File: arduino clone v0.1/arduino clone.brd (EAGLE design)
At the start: 68.6 x 26.2 mm, 47 parts, among them J203 ICSP HEADER, J402 FTDI Breakout Header, U101 ATMEGA328P_TQFP, U301 CH340G, Y101 16MHz, Y301 12MHz

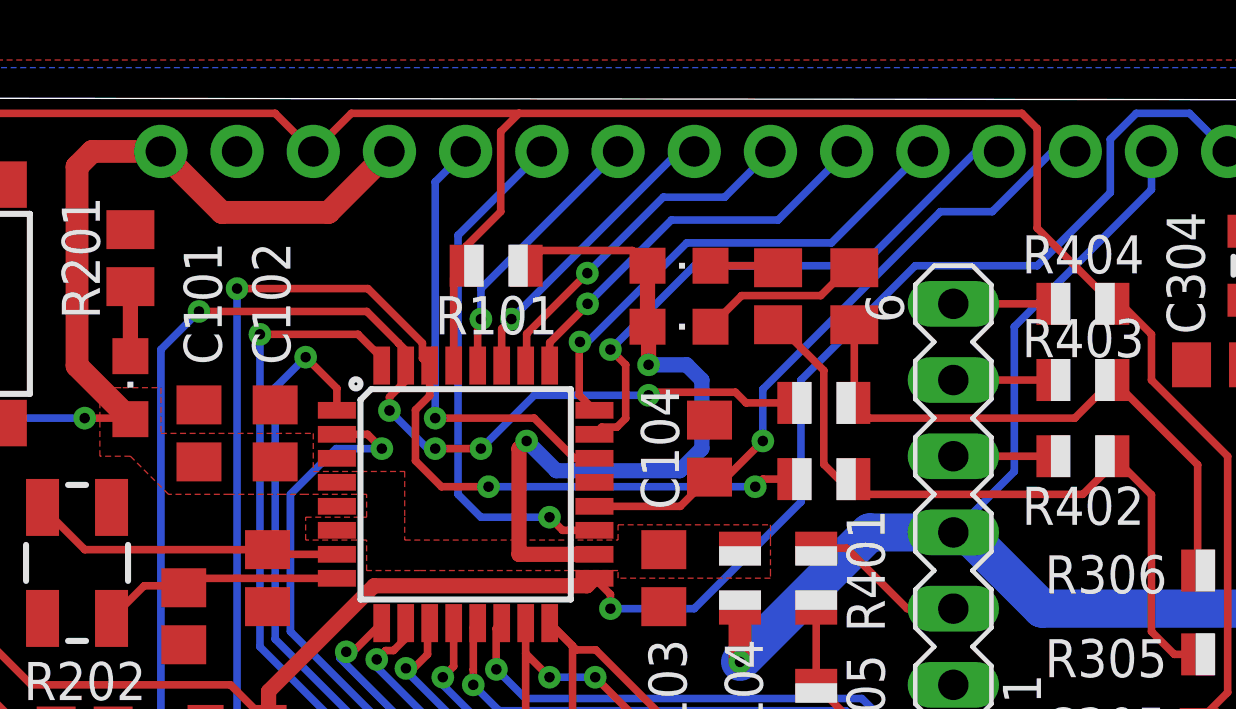
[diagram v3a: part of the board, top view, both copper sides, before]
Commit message: add gnd vias so gnd hits everything
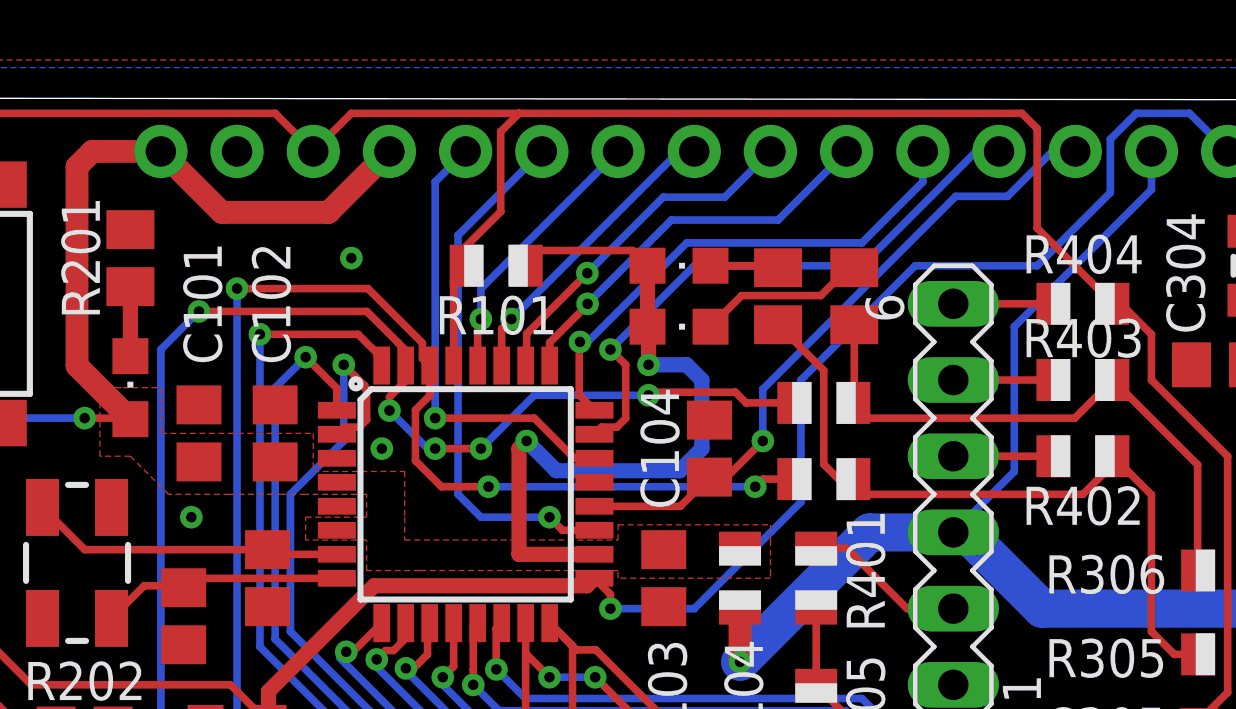
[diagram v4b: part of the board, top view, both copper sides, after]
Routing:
- net MCU_D4: track 23.7 -> 26.7 mm
- net MCU_A1: track 16.6 -> 17.2 mm
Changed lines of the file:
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@@
 <vertex x="82.042" y="66.294"/>
 </polygon>
-<wire x1="72.771" y1="50.193" x2="76.802" y2="53.37" width="0" layer="19" extent="1-1"/>
-<wire x1="70.8" y1="52.324" x2="72.771" y2="50.193" width="0" layer="19" extent="1-1"/>
-<wire x1="76.642" y1="43.942" x2="72.771" y2="50.193" width="0" layer="19" extent="1-1"/>
-<wire x1="68.85" y1="60.452" x2="70.8" y2="52.324" width="0" layer="19" extent="1-1"/>
-<wire x1="61.026" y1="53.848" x2="70.8" y2="52.324" width="0" layer="19" extent="1-1"/>
-<wire x1="58.486" y1="56.388" x2="61.026" y2="53.848" width="0" layer="19" extent="1-1"/>
-<wire x1="66.294" y1="40.402" x2="76.642" y2="43.942" width="0" layer="19" extent="1-1"/>
-<wire x1="50.546" y1="45.72" x2="61.026" y2="53.848" width="0" layer="19" extent="1-1"/>
-<wire x1="45.974" y1="43.704" x2="50.546" y2="45.72" width="0" layer="19" extent="1-1"/>
-<wire x1="40.894" y1="48.326" x2="45.974" y2="43.704" width="0" layer="19" extent="1-1"/>
+<via x="30.48" y="59.944" extent="1-16" drill="0.35"/>
+<via x="25.146" y="51.308" extent="1-16" drill="0.35"/>
+<via x="31.496" y="53.594" extent="1-16" drill="0.35"/>
 <wire x1="38.5826" y1="52.47" x2="40.894" y2="48.326" width="0" layer="19" extent="1-1"/>
-<wire x1="42.418" y1="54.544" x2="38.5826" y2="52.47" width="0" layer="19" extent="1-1"/>
-<wire x1="29.9974" y1="51.67" x2="38.5826" y2="52.47" width="0" layer="19" extent="1-1"/>
-<wire x1="29.9974" y1="53.27" x2="29.9974" y2="51.67" width="0" layer="19" extent="1-1"/>
-<wire x1="27.94" y1="55.052" x2="29.9974" y2="53.27" width="0" layer="19" extent="1-1"/>
-<wire x1="25.4" y1="55.052" x2="27.94" y2="55.052" width="0" layer="19" extent="1-1"/>
-<wire x1="27.686" y1="48.326" x2="29.9974" y2="51.67" width="0" layer="19" extent="1-1"/>
-<wire x1="24.892" y1="47.056" x2="27.686" y2="48.326" width="0" layer="19" extent="1-1"/>
-<wire x1="20.64" y1="44.196" x2="24.892" y2="47.056" width="0" layer="19" extent="1-1"/>
-<wire x1="23.114" y1="60.894" x2="25.4" y2="55.052" width="0" layer="19" extent="1-1"/>
-<wire x1="26.67" y1="63.5" x2="23.114" y2="60.894" width="0" layer="19" extent="1-1"/>
-<wire x1="14.224" y1="49.53" x2="20.64" y2="44.196" width="0" layer="19" extent="1-1"/>
-<wire x1="14.514" y1="54.445" x2="14.224" y2="49.53" width="0" layer="19" extent="1-1"/>
-<wire x1="31.75" y1="40.64" x2="27.686" y2="48.326" width="0" layer="19" extent="1-1"/>
 </signal>
 <signal name="MCU_RESET">
@@
 <via x="44.196" y="53.848" extent="1-16" drill="0.35"/>
 <wire x1="53.848" y1="63.5" x2="54.61" y2="63.5" width="0.254" layer="16"/>
-<wire x1="44.196" y1="55.5747625" x2="50.1146375" y2="61.4934" width="0.254" layer="16"/>
-<wire x1="50.1146375" y1="61.4934" x2="51.8414" y2="61.4934" width="0.254" layer="16"/>
-<wire x1="51.8414" y1="61.4934" x2="53.848" y2="63.5" width="0.254" layer="16"/>
+<wire x1="44.196" y1="55.5747625" x2="50.6226375" y2="62.0014" width="0.254" layer="16"/>
+<wire x1="50.6226375" y1="62.0014" x2="52.3494" y2="62.0014" width="0.254" layer="16"/>
+<wire x1="52.3494" y1="62.0014" x2="53.848" y2="63.5" width="0.254" layer="16"/>
 <wire x1="44.196" y1="53.848" x2="44.196" y2="55.5747625" width="0.254" layer="16"/>
 </signal>
@@
 <wire x1="38.354" y1="57.15" x2="38.1" y2="57.15" width="0.254" layer="16"/>
 <wire x1="38.354" y1="57.15" x2="41.656" y2="60.452" width="0.254" layer="16"/>
-<wire x1="46.482" y1="60.452" x2="41.656" y2="60.452" width="0.254" layer="16"/>
-<wire x1="49.53" y1="63.5" x2="46.482" y2="60.452" width="0.254" layer="16"/>
+<wire x1="47.498" y1="60.452" x2="41.656" y2="60.452" width="0.254" layer="16"/>
+<wire x1="49.53" y1="62.484" x2="47.498" y2="60.452" width="0.254" layer="16"/>
 <wire x1="38.5826" y1="54.87" x2="38.0746" y2="55.378" width="0.254" layer="1"/>
 <wire x1="38.0746" y1="57.1246" x2="38.1" y2="57.15" width="0.254" layer="1"/>
+<wire x1="49.53" y1="63.5" x2="49.53" y2="62.484" width="0.254" layer="16"/>
 </signal>
 <signal name="MCU_A2">
@@
 <contactref element="U101" pad="2"/>
 <contactref element="J201" pad="7"/>
-<wire x1="29.9974" y1="54.07" x2="31.02" y2="54.07" width="0.254" layer="1"/>
-<wire x1="31.02" y1="54.07" x2="31.496" y2="53.594" width="0.254" layer="1"/>
-<via x="31.496" y="53.594" extent="1-16" drill="0.35"/>
 <wire x1="28.448" y1="52.07" x2="28.448" y2="48.514" width="0.254" layer="16"/>
-<wire x1="29.972" y1="53.594" x2="28.448" y2="52.07" width="0.254" layer="16"/>
-<wire x1="31.496" y1="53.594" x2="29.972" y2="53.594" width="0.254" layer="16"/>
+<wire x1="30.226" y1="53.848" x2="28.448" y2="52.07" width="0.254" layer="16"/>
 <wire x1="28.448" y1="48.514" x2="28.448" y2="48.514" width="0.254" layer="16"/>
 <wire x1="28.448" y1="48.514" x2="28.448" y2="47.498" width="0.254" layer="16"/>
@@
 <wire x1="35.56" y1="42.672" x2="36.4236" y2="41.8084" width="0.254" layer="16"/>
 <wire x1="33.274" y1="42.672" x2="35.56" y2="42.672" width="0.254" layer="16"/>
+<wire x1="29.9974" y1="54.07" x2="30.2386" y2="54.3112" width="0.254" layer="1"/>
+<wire x1="30.2386" y1="54.3112" x2="30.74813125" y2="54.3112" width="0.254" layer="1"/>
+<wire x1="30.74813125" y1="54.3112" x2="30.988" y2="54.55106875" width="0.254" layer="1"/>
+<wire x1="30.988" y1="55.55506875" x2="30.9312" y2="55.61186875" width="0.254" layer="1"/>
+<wire x1="30.9312" y1="55.61186875" x2="30.9312" y2="55.6828" width="0.254" layer="1"/>
+<wire x1="30.9312" y1="55.6828" x2="30.226" y2="56.388" width="0.254" layer="1"/>
+<wire x1="30.988" y1="54.55106875" x2="30.988" y2="55.55506875" width="0.254" layer="1"/>
+<via x="30.226" y="56.388" extent="1-16" drill="0.35"/>
+<wire x1="30.226" y1="56.388" x2="30.226" y2="53.848" width="0.254" layer="16"/>
 </signal>
 <signal name="MCU_D5">

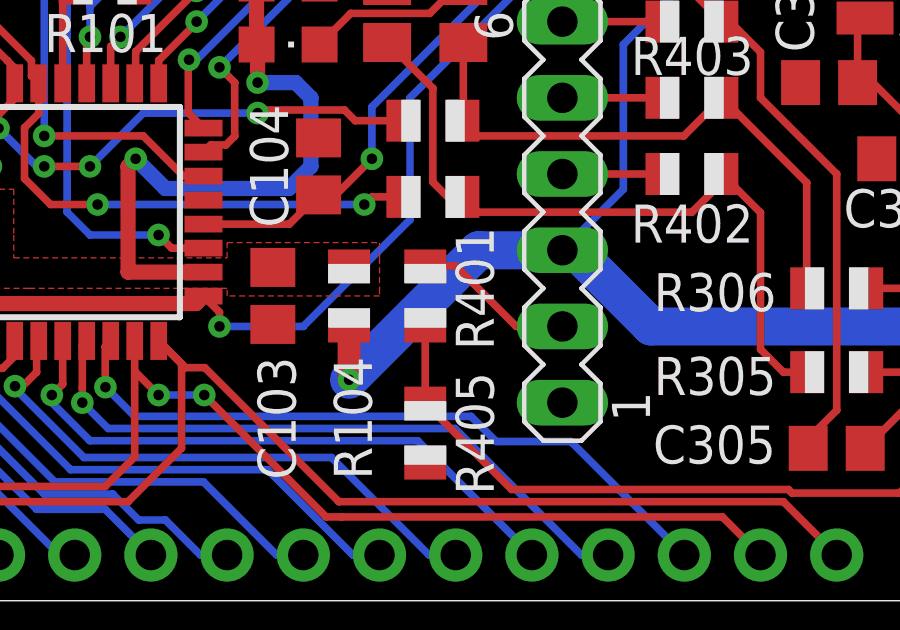
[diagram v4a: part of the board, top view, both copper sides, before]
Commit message: add shape for PP5V0_USB to MCU
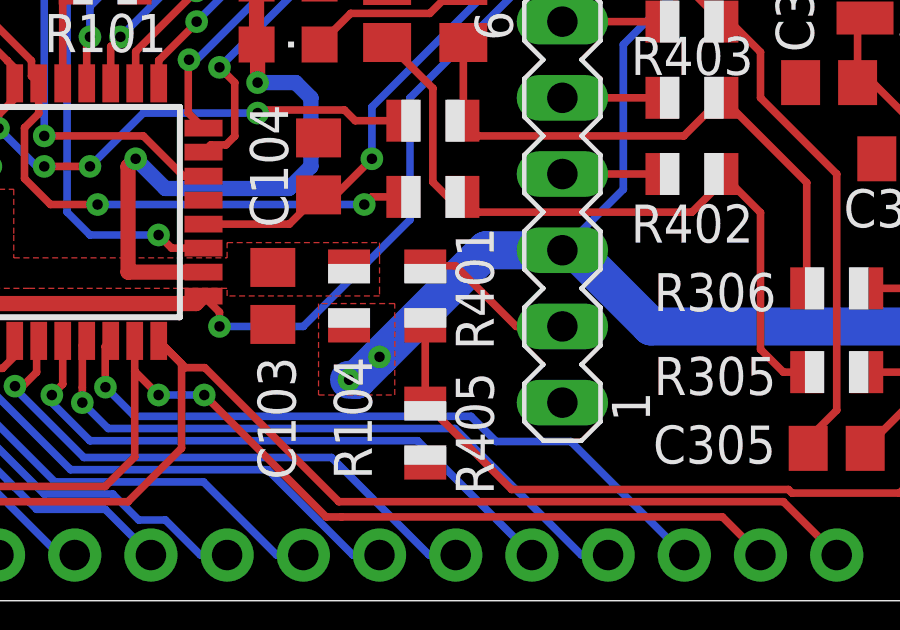
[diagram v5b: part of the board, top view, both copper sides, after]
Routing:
- net PP5V0_USB: track 65.3 -> 63.5 mm, vias 2 -> 3
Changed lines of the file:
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@@
 <via x="25.146" y="51.308" extent="1-16" drill="0.35"/>
 <via x="31.496" y="53.594" extent="1-16" drill="0.35"/>
+<wire x1="45.974" y1="43.704" x2="50.546" y2="45.72" width="0" layer="19" extent="1-1"/>
 <wire x1="38.5826" y1="52.47" x2="40.894" y2="48.326" width="0" layer="19" extent="1-1"/>
 </signal>
@@
 <vertex x="73.406" y="47.498"/>
 </polygon>
-<wire x1="43.434" y1="48.276" x2="43.434" y2="46.482" width="0.762" layer="1"/>
 <via x="43.434" y="46.482" extent="1-16" drill="0.35"/>
-<wire x1="43.434" y1="46.482" x2="47.752" y2="50.8" width="1.27" layer="16"/>
-<wire x1="47.752" y1="50.8" x2="50.546" y2="50.8" width="1.27" layer="16"/>
+<wire x1="43.688" y1="46.482" x2="44.45" y2="47.244" width="1.27" layer="16"/>
+<wire x1="44.45" y1="47.244" x2="48.006" y2="50.8" width="1.27" layer="16"/>
+<wire x1="48.006" y1="50.8" x2="50.546" y2="50.8" width="1.27" layer="16"/>
 <wire x1="74.676" y1="48.498" x2="72.628" y2="48.498" width="1.27" layer="1"/>
 <wire x1="72.628" y1="48.498" x2="72.39" y2="48.26" width="1.27" layer="1"/>
@@
 <wire x1="78.108" y1="59.036" x2="78.108" y2="49.83614375" width="0.254" layer="1"/>
 <wire x1="76.692" y1="60.452" x2="78.108" y2="59.036" width="0.254" layer="1"/>
+<via x="44.45" y="47.244" extent="1-16" drill="0.35"/>
+<wire x1="43.434" y1="46.482" x2="43.688" y2="46.482" width="1.27" layer="16"/>
+<polygon width="0.0762" layer="1">
+<vertex x="42.418" y="49.022"/>
+<vertex x="42.418" y="45.974"/>
+<vertex x="44.958" y="45.974"/>
+<vertex x="44.958" y="49.022"/>
+</polygon>
 </signal>
 <signal name="PP5V0_CH340G">

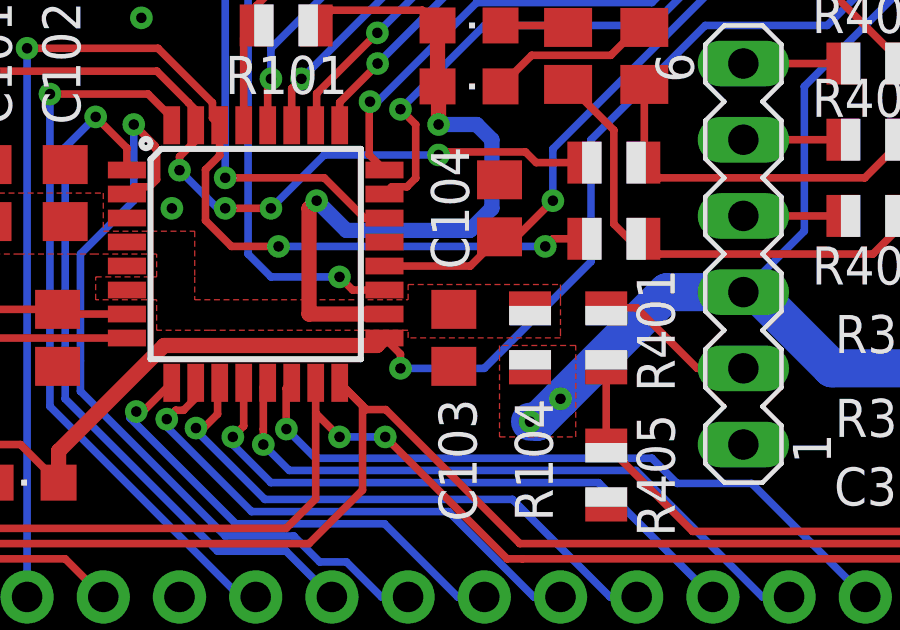
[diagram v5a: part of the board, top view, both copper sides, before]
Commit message: add gnd vias so gnd hits everything
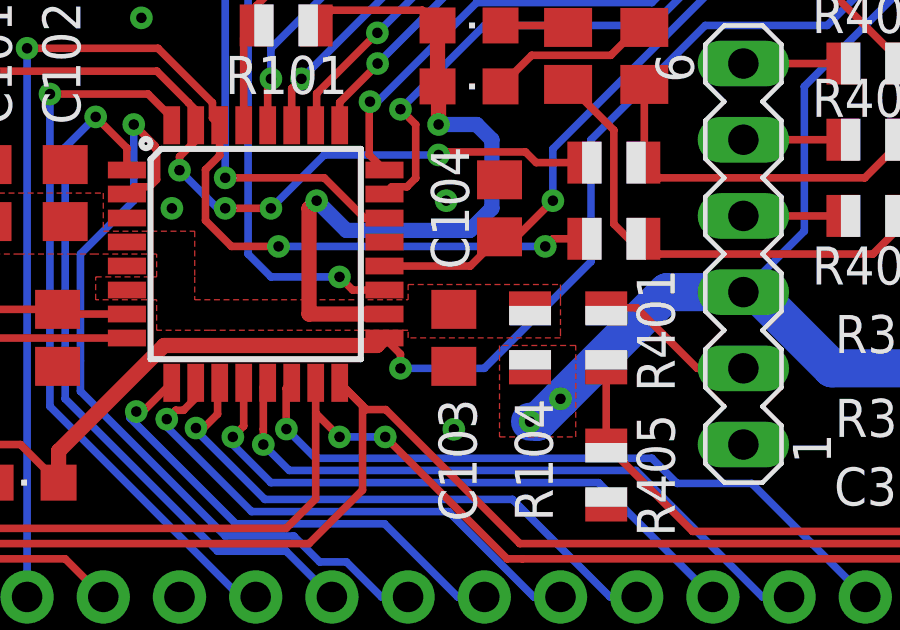
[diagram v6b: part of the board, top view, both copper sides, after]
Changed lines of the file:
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@@
 <via x="25.146" y="51.308" extent="1-16" drill="0.35"/>
 <via x="31.496" y="53.594" extent="1-16" drill="0.35"/>
+<via x="40.894" y="46.228" extent="1-16" drill="0.35"/>
+<via x="40.64" y="53.848" extent="1-16" drill="0.35"/>
+<wire x1="72.771" y1="50.193" x2="76.802" y2="53.37" width="0" layer="19" extent="1-1"/>
+<wire x1="70.8" y1="52.324" x2="72.771" y2="50.193" width="0" layer="19" extent="1-1"/>
+<wire x1="76.642" y1="43.942" x2="72.771" y2="50.193" width="0" layer="19" extent="1-1"/>
+<wire x1="68.85" y1="60.452" x2="70.8" y2="52.324" width="0" layer="19" extent="1-1"/>
+<wire x1="61.026" y1="53.848" x2="70.8" y2="52.324" width="0" layer="19" extent="1-1"/>
+<wire x1="58.486" y1="56.388" x2="61.026" y2="53.848" width="0" layer="19" extent="1-1"/>
+<wire x1="66.294" y1="40.402" x2="76.642" y2="43.942" width="0" layer="19" extent="1-1"/>
+<wire x1="50.546" y1="45.72" x2="61.026" y2="53.848" width="0" layer="19" extent="1-1"/>
 <wire x1="45.974" y1="43.704" x2="50.546" y2="45.72" width="0" layer="19" extent="1-1"/>
+<wire x1="40.894" y1="46.228" x2="45.974" y2="43.704" width="0" layer="19" extent="1-1"/>
+<wire x1="40.894" y1="48.326" x2="40.894" y2="46.228" width="0" layer="19" extent="1-1"/>
 <wire x1="38.5826" y1="52.47" x2="40.894" y2="48.326" width="0" layer="19" extent="1-1"/>
+<wire x1="40.64" y1="53.848" x2="38.5826" y2="52.47" width="0" layer="19" extent="1-1"/>
+<wire x1="42.418" y1="54.544" x2="40.64" y2="53.848" width="0" layer="19" extent="1-1"/>
+<wire x1="31.496" y1="53.594" x2="38.5826" y2="52.47" width="0" layer="19" extent="1-1"/>
+<wire x1="29.9974" y1="53.27" x2="31.496" y2="53.594" width="0" layer="19" extent="1-1"/>
+<wire x1="29.9974" y1="51.67" x2="29.9974" y2="53.27" width="0" layer="19" extent="1-1"/>
+<wire x1="27.94" y1="55.052" x2="29.9974" y2="53.27" width="0" layer="19" extent="1-1"/>
+<wire x1="25.4" y1="55.052" x2="27.94" y2="55.052" width="0" layer="19" extent="1-1"/>
+<wire x1="25.146" y1="51.308" x2="25.4" y2="55.052" width="0" layer="19" extent="1-1"/>
+<wire x1="27.686" y1="48.326" x2="25.146" y2="51.308" width="0" layer="19" extent="1-1"/>
+<wire x1="24.892" y1="47.056" x2="27.686" y2="48.326" width="0" layer="19" extent="1-1"/>
+<wire x1="20.64" y1="44.196" x2="24.892" y2="47.056" width="0" layer="19" extent="1-1"/>
+<wire x1="30.48" y1="59.944" x2="27.94" y2="55.052" width="0" layer="19" extent="1-1"/>
+<wire x1="26.67" y1="63.5" x2="30.48" y2="59.944" width="0" layer="19" extent="1-1"/>
+<wire x1="23.114" y1="60.894" x2="26.67" y2="63.5" width="0" layer="19" extent="1-1"/>
+<wire x1="14.224" y1="49.53" x2="20.64" y2="44.196" width="0" layer="19" extent="1-1"/>
+<wire x1="14.514" y1="54.445" x2="14.224" y2="49.53" width="0" layer="19" extent="1-1"/>
+<wire x1="31.75" y1="40.64" x2="27.686" y2="48.326" width="0" layer="19" extent="1-1"/>
 </signal>
 <signal name="MCU_RESET">
